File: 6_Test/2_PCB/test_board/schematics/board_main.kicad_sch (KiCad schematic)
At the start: 3 parts

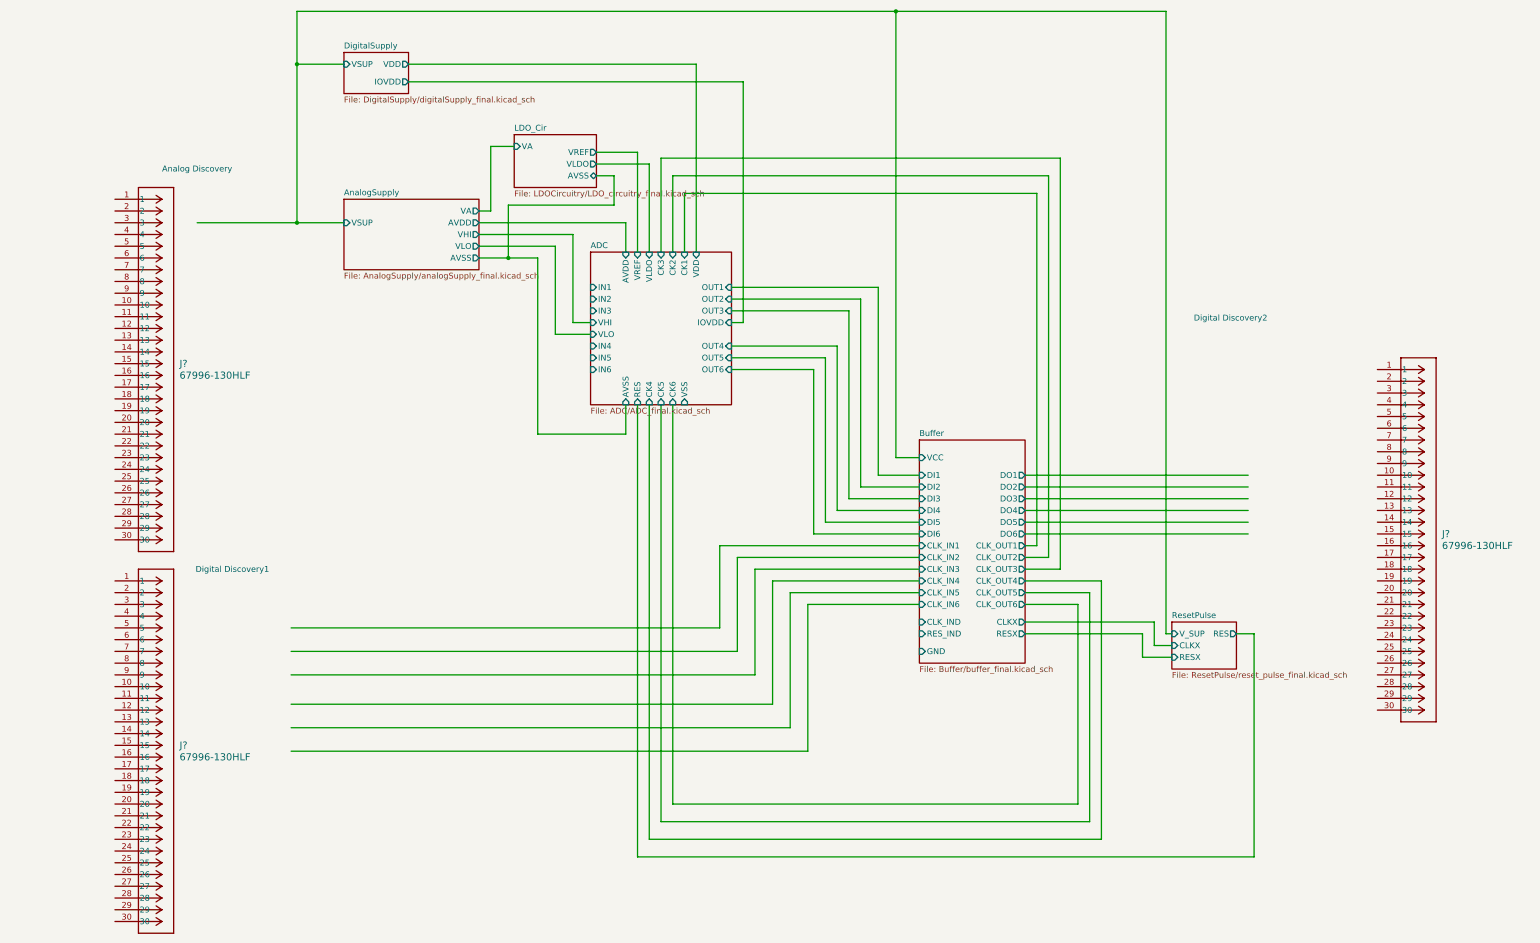
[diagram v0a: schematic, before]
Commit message: fixed analog input wires
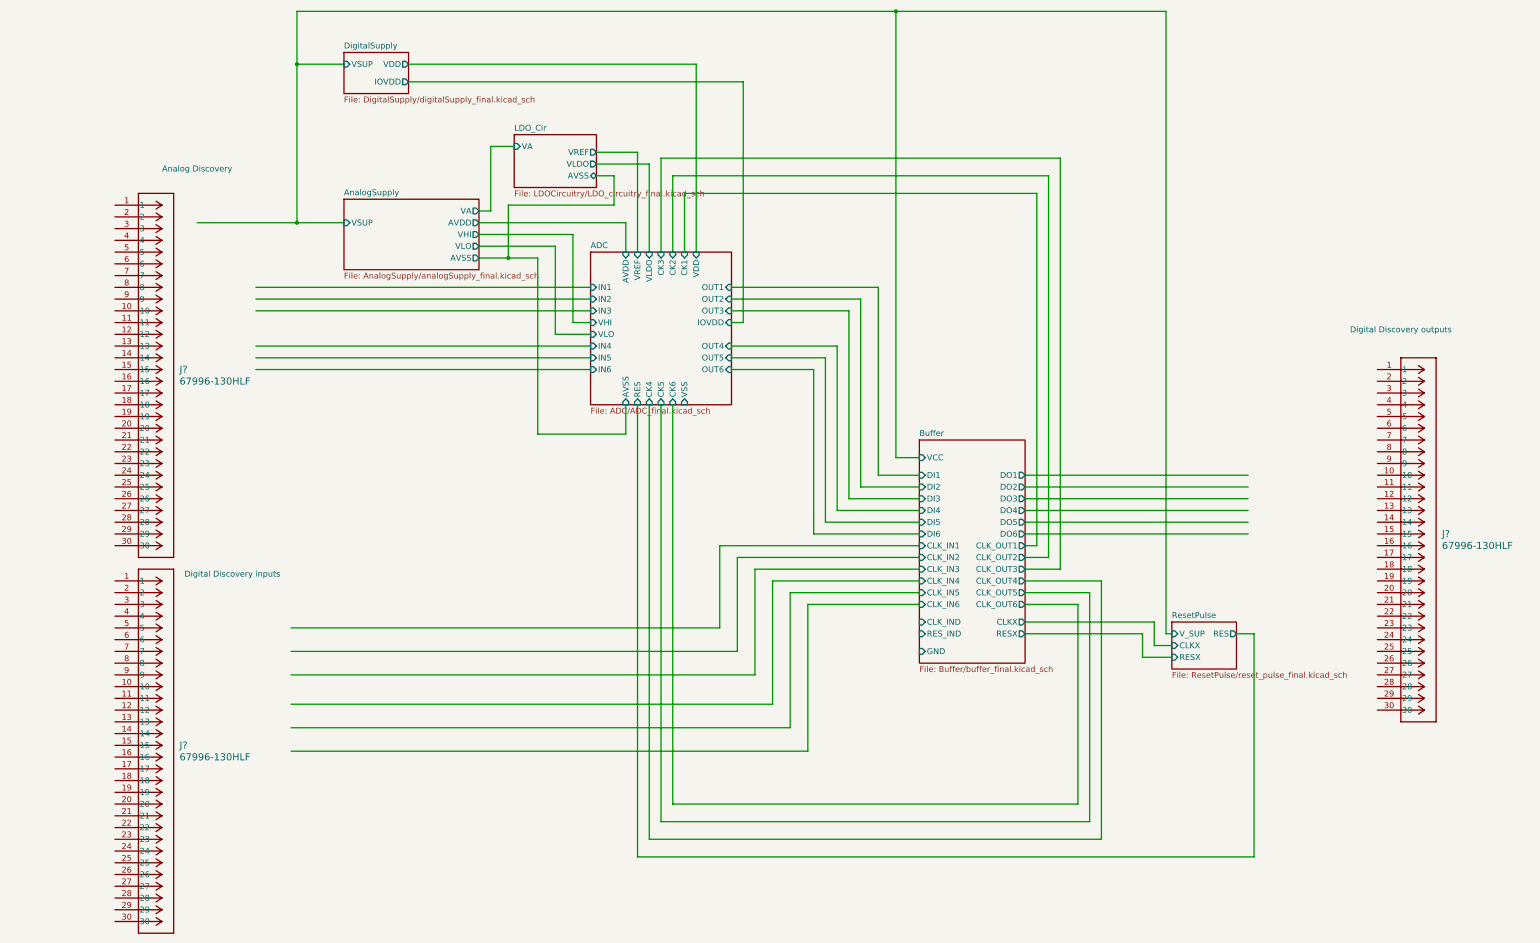
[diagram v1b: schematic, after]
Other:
- note added: "Digital Discovery inputs"
- note added: "Digital Discovery outputs"
- note removed: "Digital Discovery1"
- note removed: "Digital Discovery2"
- moved on the sheet: J?
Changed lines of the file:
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@@
+	(wire
+		(pts
+			(xy 121.92 106.68) (xy 194.31 106.68)
+		)
+		(stroke
+			(width 0)
+			(type default)
+		)
+	)
 	(wire
 		(pts
@@
 	(wire
 		(pts
+			(xy 121.92 109.22) (xy 194.31 109.22)
+		)
+		(stroke
+			(width 0)
+			(type default)
+		)
+	)
+	(wire
+		(pts
 			(xy 172.72 90.17) (xy 170.18 90.17)
 		)
@@
 	(wire
 		(pts
+			(xy 121.92 121.92) (xy 194.31 121.92)
+		)
+		(stroke
+			(width 0)
+			(type default)
+		)
+	)
+	(wire
+		(pts
 			(xy 288.29 165.1) (xy 293.37 165.1)
 		)
@@
 	(wire
 		(pts
+			(xy 121.92 111.76) (xy 194.31 111.76)
+		)
+		(stroke
+			(width 0)
+			(type default)
+		)
+	)
+	(wire
+		(pts
 			(xy 170.18 95.25) (xy 190.5 95.25)
 		)
@@
 	(wire
 		(pts
+			(xy 121.92 124.46) (xy 194.31 124.46)
+		)
+		(stroke
+			(width 0)
+			(type default)
+		)
+	)
+	(wire
+		(pts
 			(xy 209.55 78.74) (xy 209.55 99.06)
 		)
@@
 		(pts
 			(xy 265.43 170.18) (xy 233.68 170.18)
+		)
+		(stroke
+			(width 0)
+			(type default)
+		)
+	)
+	(wire
+		(pts
+			(xy 121.92 119.38) (xy 194.31 119.38)
 		)
 		(stroke
@@
 		)
 	)
-	(text "Digital Discovery2\n\n\n"
+	(text "Digital Discovery outputs\n\n\n"
 		(exclude_from_sim no)
-		(at 332.74 115.57 0)
+		(at 369.57 118.11 0)
 		(effects
 			(font
@@
 		)
 	)
-	(text "Digital Discovery1\n\n"
+	(text "Digital Discovery inputs\n"
 		(exclude_from_sim no)
 		(at 116.84 168.91 0)
@@
 	(symbol
 		(lib_id "15x2Header:67996-130HLF")
-		(at 91.44 87.63 0)
+		(at 91.44 88.9 0)
 		(unit 1)
 		(exclude_from_sim no)
@@
 		(fields_autoplaced yes)
 		(property "Reference" "J?"
-			(at 105.41 123.1899 0)
+			(at 105.41 124.4599 0)
 			(effects
 				(font
@@
 		)
 		(property "Value" "67996-130HLF"
-			(at 105.41 125.7299 0)
+			(at 105.41 126.9999 0)
 			(effects
 				(font
@@
 		)
 		(property "Footprint" "67996-130HLF_AMP"
-			(at 91.44 87.63 0)
+			(at 91.44 88.9 0)
 			(effects
 				(font
@@
 		)
 		(property "Datasheet" "67996-130HLF"
-			(at 91.44 87.63 0)
+			(at 91.44 88.9 0)
 			(effects
 				(font
@@
 		)
 		(property "Description" ""
-			(at 91.44 87.63 0)
+			(at 91.44 88.9 0)
 			(effects
 				(font

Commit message: made changes with accordance to feedback. Remvoed excess files.
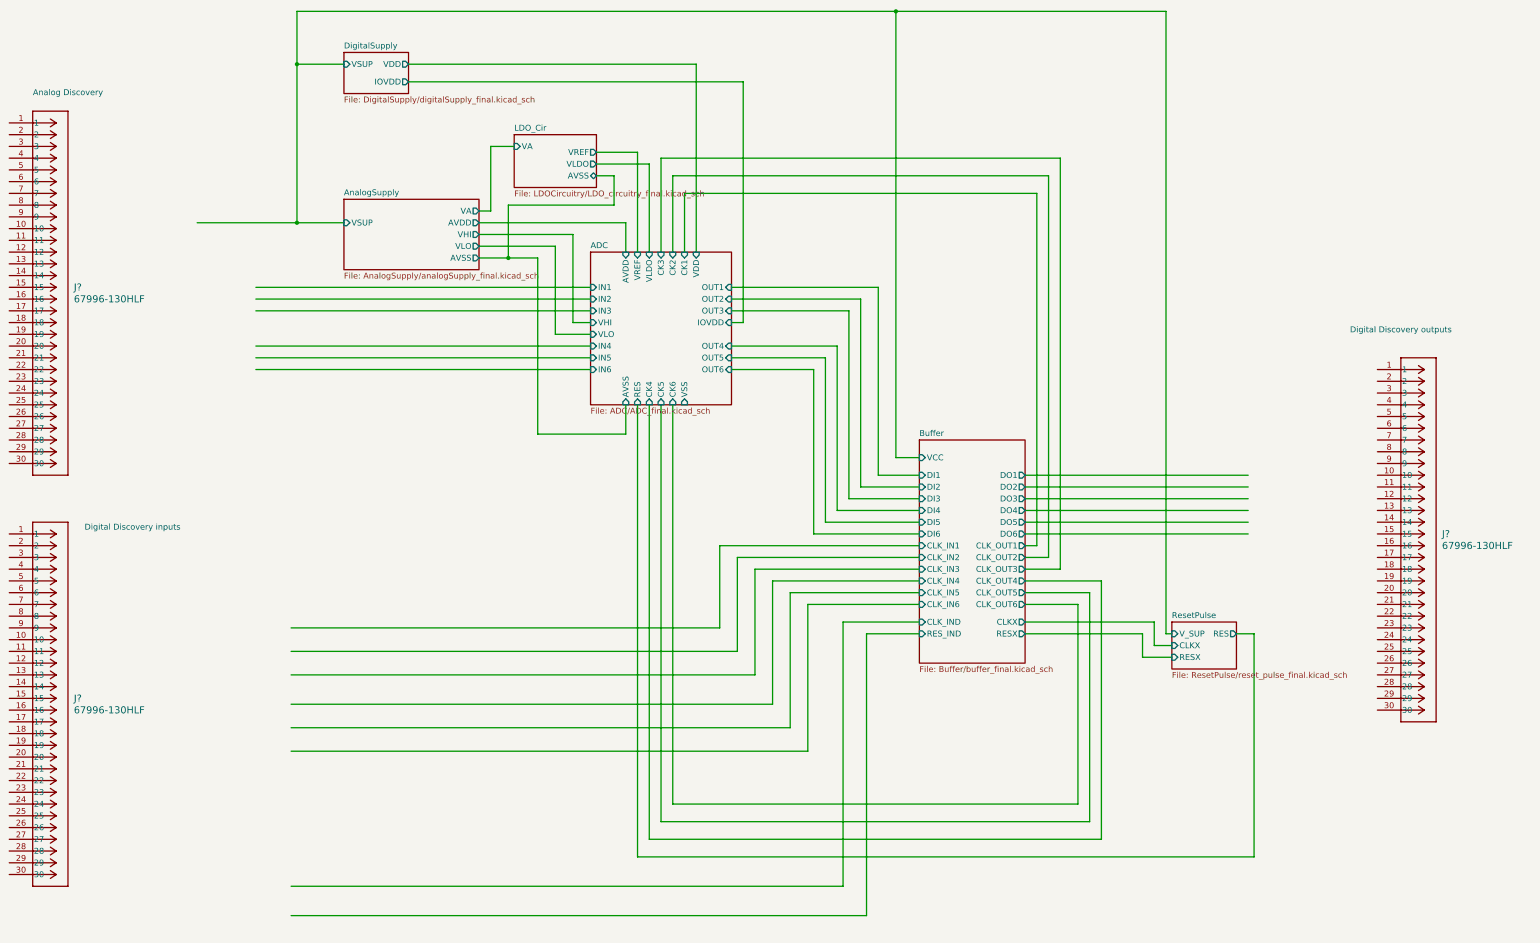
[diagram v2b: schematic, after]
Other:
- sheet Buffer ports: added none; removed GND
- moved on the sheet: J?
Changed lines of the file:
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@@
+	(wire
+		(pts
+			(xy 248.92 179.07) (xy 248.92 236.22)
+		)
+		(stroke
+			(width 0)
+			(type default)
+		)
+	)
 	(wire
 		(pts
@@
 	(wire
 		(pts
+			(xy 254 181.61) (xy 254 242.57)
+		)
+		(stroke
+			(width 0)
+			(type default)
+		)
+	)
+	(wire
+		(pts
 			(xy 288.29 167.64) (xy 295.91 167.64)
 		)
@@
 	(wire
 		(pts
+			(xy 129.54 242.57) (xy 254 242.57)
+		)
+		(stroke
+			(width 0)
+			(type default)
+		)
+	)
+	(wire
+		(pts
 			(xy 288.29 157.48) (xy 336.55 157.48)
 		)
@@
 	(wire
 		(pts
+			(xy 129.54 236.22) (xy 248.92 236.22)
+		)
+		(stroke
+			(width 0)
+			(type default)
+		)
+	)
+	(wire
+		(pts
 			(xy 245.11 121.92) (xy 245.11 157.48)
 		)
@@
 	(wire
 		(pts
+			(xy 265.43 181.61) (xy 254 181.61)
+		)
+		(stroke
+			(width 0)
+			(type default)
+		)
+	)
+	(wire
+		(pts
 			(xy 229.87 167.64) (xy 229.87 190.5)
 		)
@@
 		(pts
 			(xy 256.54 106.68) (xy 256.54 147.32)
+		)
+		(stroke
+			(width 0)
+			(type default)
+		)
+	)
+	(wire
+		(pts
+			(xy 265.43 179.07) (xy 248.92 179.07)
 		)
 		(stroke
@@
 	(text "Analog Discovery"
 		(exclude_from_sim no)
-		(at 109.22 81.28 0)
+		(at 81.28 64.77 0)
 		(effects
 			(font
@@
 	(text "Digital Discovery inputs\n"
 		(exclude_from_sim no)
-		(at 116.84 168.91 0)
+		(at 95.25 158.75 0)
 		(effects
 			(font
@@
 	(symbol
 		(lib_id "15x2Header:67996-130HLF")
-		(at 91.44 88.9 0)
+		(at 68.58 71.12 0)
 		(unit 1)
 		(exclude_from_sim no)
@@
 		(fields_autoplaced yes)
 		(property "Reference" "J?"
-			(at 105.41 124.4599 0)
+			(at 82.55 106.6799 0)
 			(effects
 				(font
@@
 		)
 		(property "Value" "67996-130HLF"
-			(at 105.41 126.9999 0)
+			(at 82.55 109.2199 0)
 			(effects
 				(font
@@
 		)
 		(property "Footprint" "67996-130HLF_AMP"
-			(at 91.44 88.9 0)
+			(at 68.58 71.12 0)
 			(effects
 				(font
@@
 		)
 		(property "Datasheet" "67996-130HLF"
-			(at 91.44 88.9 0)
+			(at 68.58 71.12 0)
 			(effects
 				(font
@@
 		)
 		(property "Description" ""
-			(at 91.44 88.9 0)
+			(at 68.58 71.12 0)
 			(effects
 				(font
@@
 	(symbol
 		(lib_id "15x2Header:67996-130HLF")
-		(at 91.44 170.18 0)
+		(at 68.58 160.02 0)
 		(unit 1)
 		(exclude_from_sim no)
@@
 		(fields_autoplaced yes)
 		(property "Reference" "J?"
-			(at 105.41 205.7399 0)
+			(at 82.55 195.5799 0)
 			(effects
 				(font
@@
 		)
 		(property "Value" "67996-130HLF"
-			(at 105.41 208.2799 0)
+			(at 82.55 198.1199 0)
 			(effects
 				(font
@@
 		)
 		(property "Footprint" "67996-130HLF_AMP"
-			(at 91.44 170.18 0)
+			(at 68.58 160.02 0)
 			(effects
 				(font
@@
 		)
 		(property "Datasheet" "67996-130HLF"
-			(at 91.44 170.18 0)
+			(at 68.58 160.02 0)
 			(effects
 				(font
@@
 		)
 		(property "Description" ""
-			(at 91.44 170.18 0)
+			(at 68.58 160.02 0)
 			(effects
 				(font
@@
 			(effects
 				(font
-					(size 1.27 1.27)
-				)
-				(justify left)
-			)
-		)
-		(pin "GND" input
-			(at 265.43 185.42 180)
-			(effects
-				(font
